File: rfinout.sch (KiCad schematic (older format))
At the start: 4 parts

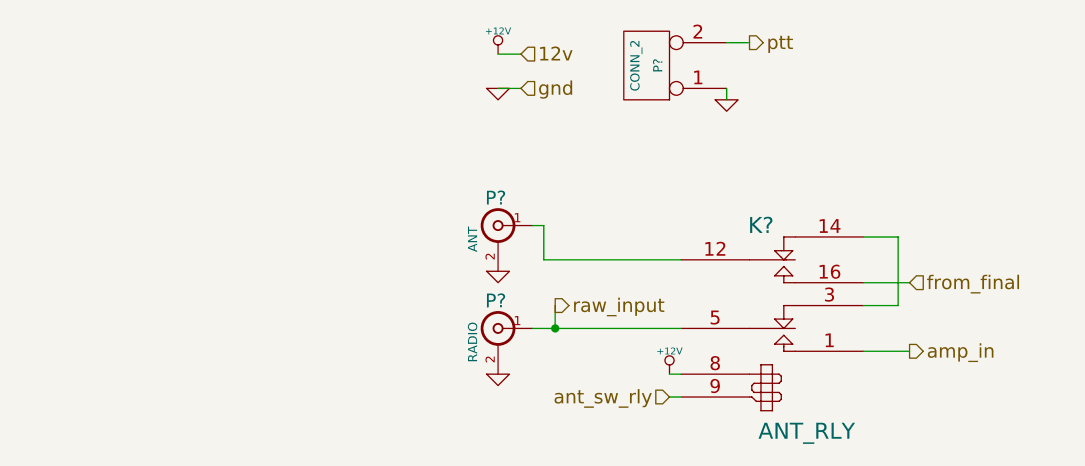
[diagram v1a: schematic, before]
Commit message: Annotated all schematics
- Added more caps to power supply
- Decided on power supply fuse part
- Changed 1n5711 SWR caps to BAT62
- Decided on MMBF170 for amp bias switch
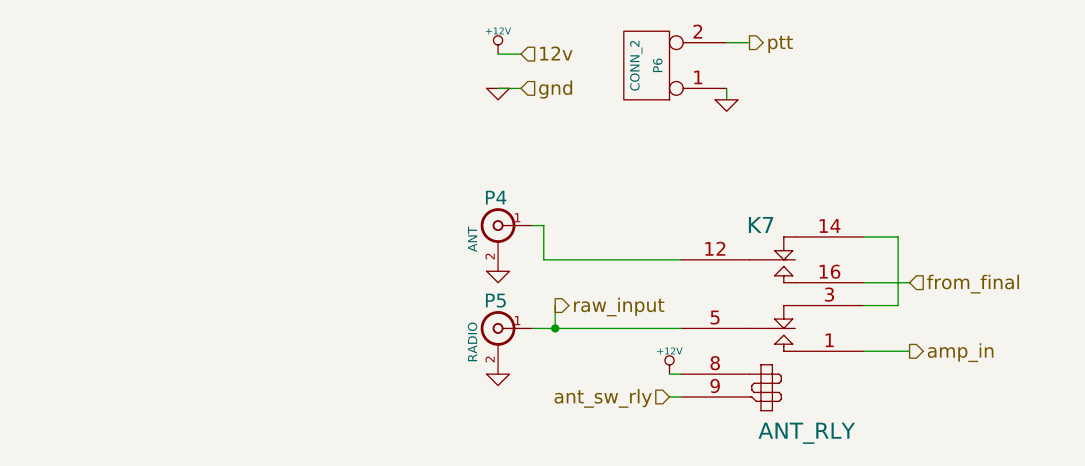
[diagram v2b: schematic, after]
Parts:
- gave numbers to parts that had none: 4
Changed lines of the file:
@@
 $EndDescr
 $Comp
-L BNC P?
+L BNC P5
 U 1 1 5472C36C
 P 5150 3750
-F 0 "P?" H 5160 3870 60  0000 C CNN
+F 0 "P5" H 5160 3870 60  0000 C CNN
 F 1 "RADIO" V 5260 3690 40  0000 C CNN
 F 2 "" H 5150 3750 60  0000 C CNN
@@
 $EndComp
 $Comp
-L BNC P?
+L BNC P4
 U 1 1 5472C37E
 P 5150 3300
-F 0 "P?" H 5160 3420 60  0000 C CNN
+F 0 "P4" H 5160 3420 60  0000 C CNN
 F 1 "ANT" V 5260 3240 40  0000 C CNN
 F 2 "" H 5150 3300 60  0000 C CNN
@@
 $EndComp
 $Comp
-L RELAY_2RT K?
+L RELAY_2RT K7
 U 1 1 5472C38B
 P 6350 3700
-F 0 "K?" H 6300 4100 70  0000 C CNN
+F 0 "K7" H 6300 4100 70  0000 C CNN
 F 1 "ANT_RLY" H 6500 3200 70  0000 C CNN
 F 2 "" H 6350 3700 60  0000 C CNN
@@
 $EndComp
 $Comp
-L +12V #PWR?
+L +12V #PWR100
 U 1 1 5472C39F
 P 5900 3950
-F 0 "#PWR?" H 5900 3900 20  0001 C CNN
+F 0 "#PWR100" H 5900 3900 20  0001 C CNN
 F 1 "+12V" H 5900 4050 30  0000 C CNN
 F 2 "" H 5900 3950 60  0000 C CNN
@@
 ant_sw_rly
 $Comp
-L GND #PWR?
+L GND #PWR99
 U 1 1 5472C3BF
 P 5150 3950
-F 0 "#PWR?" H 5150 3950 30  0001 C CNN
+F 0 "#PWR99" H 5150 3950 30  0001 C CNN
 F 1 "GND" H 5150 3880 30  0001 C CNN
 F 2 "" H 5150 3950 60  0000 C CNN
@@
 $EndComp
 $Comp
-L GND #PWR?
+L GND #PWR98
 U 1 1 5472C3D3
 P 5150 3500
-F 0 "#PWR?" H 5150 3500 30  0001 C CNN
+F 0 "#PWR98" H 5150 3500 30  0001 C CNN
 F 1 "GND" H 5150 3430 30  0001 C CNN
 F 2 "" H 5150 3500 60  0000 C CNN
@@
 from_final
 $Comp
-L GND #PWR?
+L GND #PWR97
 U 1 1 5472C7C7
 P 5150 2700
-F 0 "#PWR?" H 5150 2700 30  0001 C CNN
+F 0 "#PWR97" H 5150 2700 30  0001 C CNN
 F 1 "GND" H 5150 2630 30  0001 C CNN
 F 2 "" H 5150 2700 60  0000 C CNN
@@
 $EndComp
 $Comp
-L +12V #PWR?
+L +12V #PWR96
 U 1 1 5472C7D2
 P 5150 2550
-F 0 "#PWR?" H 5150 2500 20  0001 C CNN
+F 0 "#PWR96" H 5150 2500 20  0001 C CNN
 F 1 "+12V" H 5150 2650 30  0000 C CNN
 F 2 "" H 5150 2550 60  0000 C CNN
@@
 Connection ~ 5400 3750
 $Comp
-L CONN_2 P?
+L CONN_2 P6
 U 1 1 5472CC33
 P 5800 2600
-F 0 "P?" V 5750 2600 40  0000 C CNN
+F 0 "P6" V 5750 2600 40  0000 C CNN
 F 1 "CONN_2" V 5850 2600 40  0000 C CNN
 F 2 "" H 5800 2600 60  0000 C CNN
@@
 $EndComp
 $Comp
-L GND #PWR?
+L GND #PWR101
 U 1 1 5472CC45
 P 6150 2750
-F 0 "#PWR?" H 6150 2750 30  0001 C CNN
+F 0 "#PWR101" H 6150 2750 30  0001 C CNN
 F 1 "GND" H 6150 2680 30  0001 C CNN
 F 2 "" H 6150 2750 60  0000 C CNN

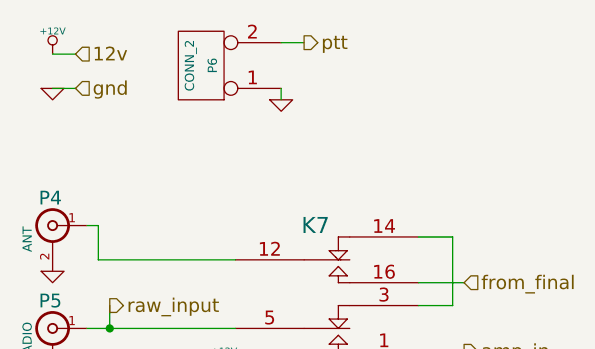
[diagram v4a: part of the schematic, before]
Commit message: Finished associating relays
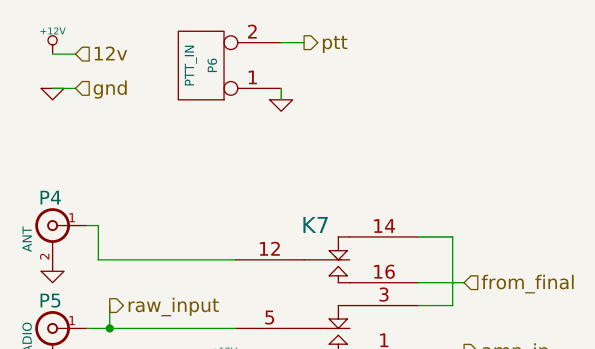
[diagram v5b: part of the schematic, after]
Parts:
- P6: value CONN_2 -> PTT_IN
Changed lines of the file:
@@
 LIBS:mcus
 LIBS:transformers
+LIBS:relays
 LIBS:qrpamp-cache
 EELAYER 25 0
@@
 $EndComp
 $Comp
-L RELAY_2RT K7
-U 1 1 5472C38B
-P 6350 3700
-F 0 "K7" H 6300 4100 70  0000 C CNN
-F 1 "ANT_RLY" H 6500 3200 70  0000 C CNN
-F 2 "" H 6350 3700 60  0001 C CNN
-F 3 "" H 6350 3700 60  0000 C CNN
-	1    6350 3700
-	1    0    0    -1
-$EndComp
-$Comp
-L +12V #PWR096
+L +12V #PWR99
 U 1 1 5472C39F
 P 5900 3950
-F 0 "#PWR096" H 5900 3900 20  0001 C CNN
+F 0 "#PWR99" H 5900 3900 20  0001 C CNN
 F 1 "+12V" H 5900 4050 30  0000 C CNN
 F 2 "" H 5900 3950 60  0000 C CNN
@@
 ant_sw_rly
 $Comp
-L GND #PWR097
+L GND #PWR98
 U 1 1 5472C3BF
 P 5150 3950
-F 0 "#PWR097" H 5150 3950 30  0001 C CNN
+F 0 "#PWR98" H 5150 3950 30  0001 C CNN
 F 1 "GND" H 5150 3880 30  0001 C CNN
 F 2 "" H 5150 3950 60  0000 C CNN
@@
 $EndComp
 $Comp
-L GND #PWR098
+L GND #PWR97
 U 1 1 5472C3D3
 P 5150 3500
-F 0 "#PWR098" H 5150 3500 30  0001 C CNN
+F 0 "#PWR97" H 5150 3500 30  0001 C CNN
 F 1 "GND" H 5150 3430 30  0001 C CNN
 F 2 "" H 5150 3500 60  0000 C CNN
@@
 from_final
 $Comp
-L GND #PWR099
+L GND #PWR96
 U 1 1 5472C7C7
 P 5150 2700
-F 0 "#PWR099" H 5150 2700 30  0001 C CNN
+F 0 "#PWR96" H 5150 2700 30  0001 C CNN
 F 1 "GND" H 5150 2630 30  0001 C CNN
 F 2 "" H 5150 2700 60  0000 C CNN
@@
 $EndComp
 $Comp
-L +12V #PWR0100
+L +12V #PWR95
 U 1 1 5472C7D2
 P 5150 2550
-F 0 "#PWR0100" H 5150 2500 20  0001 C CNN
+F 0 "#PWR95" H 5150 2500 20  0001 C CNN
 F 1 "+12V" H 5150 2650 30  0000 C CNN
 F 2 "" H 5150 2550 60  0000 C CNN
@@
 P 5800 2600
 F 0 "P6" V 5750 2600 40  0000 C CNN
-F 1 "CONN_2" V 5850 2600 40  0000 C CNN
+F 1 "PTT_IN" V 5850 2600 40  0000 C CNN
 F 2 "" H 5800 2600 60  0001 C CNN
 F 3 "" H 5800 2600 60  0000 C CNN
@@
 $EndComp
 $Comp
-L GND #PWR0101
+L GND #PWR100
 U 1 1 5472CC45
 P 6150 2750
-F 0 "#PWR0101" H 6150 2750 30  0001 C CNN
+F 0 "#PWR100" H 6150 2750 30  0001 C CNN
 F 1 "GND" H 6150 2680 30  0001 C CNN
 F 2 "" H 6150 2750 60  0000 C CNN
@@
 Text HLabel 6250 2500 2    60   Output ~ 0
 ptt
+$Comp
+L RELAY_2RT K7
+U 1 1 547A886B
+P 6350 3700
+F 0 "K7" H 6300 4100 70  0000 C CNN
+F 1 "ANT_RLY" H 6500 3200 70  0000 C CNN
+F 2 "" H 6350 3700 60  0000 C CNN
+F 3 "" H 6350 3700 60  0000 C CNN
+	1    6350 3700
+	1    0    0    -1
+$EndComp
 $EndSCHEMATC

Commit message: Everything associated except joystick
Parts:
- K7: footprint (none) -> nu9j-footprints:EC2-12NU
- P4, P5: footprint (none) -> nu9j-footprints:SMA-EDGE-0.375in
- P6: footprint (none) -> nu9j-footprints:3.5MM_SWITCHCRAFT-35RASMT2AHNTRX
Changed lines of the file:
@@
 F 0 "P5" H 5160 3870 60  0000 C CNN
 F 1 "RADIO" V 5260 3690 40  0000 C CNN
-F 2 "" H 5150 3750 60  0001 C CNN
+F 2 "nu9j-footprints:SMA-EDGE-0.375in" H 5150 3750 60  0001 C CNN
 F 3 "" H 5150 3750 60  0000 C CNN
 	1    5150 3750
@@
 F 0 "P4" H 5160 3420 60  0000 C CNN
 F 1 "ANT" V 5260 3240 40  0000 C CNN
-F 2 "" H 5150 3300 60  0001 C CNN
+F 2 "nu9j-footprints:SMA-EDGE-0.375in" H 5150 3300 60  0001 C CNN
 F 3 "" H 5150 3300 60  0000 C CNN
 	1    5150 3300
@@
 $EndComp
 $Comp
-L +12V #PWR99
+L +12V #PWR095
 U 1 1 5472C39F
 P 5900 3950
-F 0 "#PWR99" H 5900 3900 20  0001 C CNN
+F 0 "#PWR095" H 5900 3900 20  0001 C CNN
 F 1 "+12V" H 5900 4050 30  0000 C CNN
 F 2 "" H 5900 3950 60  0000 C CNN
@@
 ant_sw_rly
 $Comp
-L GND #PWR98
+L GND #PWR096
 U 1 1 5472C3BF
 P 5150 3950
-F 0 "#PWR98" H 5150 3950 30  0001 C CNN
+F 0 "#PWR096" H 5150 3950 30  0001 C CNN
 F 1 "GND" H 5150 3880 30  0001 C CNN
 F 2 "" H 5150 3950 60  0000 C CNN
@@
 $EndComp
 $Comp
-L GND #PWR97
+L GND #PWR097
 U 1 1 5472C3D3
 P 5150 3500
-F 0 "#PWR97" H 5150 3500 30  0001 C CNN
+F 0 "#PWR097" H 5150 3500 30  0001 C CNN
 F 1 "GND" H 5150 3430 30  0001 C CNN
 F 2 "" H 5150 3500 60  0000 C CNN
@@
 from_final
 $Comp
-L GND #PWR96
+L GND #PWR098
 U 1 1 5472C7C7
 P 5150 2700
-F 0 "#PWR96" H 5150 2700 30  0001 C CNN
+F 0 "#PWR098" H 5150 2700 30  0001 C CNN
 F 1 "GND" H 5150 2630 30  0001 C CNN
 F 2 "" H 5150 2700 60  0000 C CNN
@@
 $EndComp
 $Comp
-L +12V #PWR95
+L +12V #PWR099
 U 1 1 5472C7D2
 P 5150 2550
-F 0 "#PWR95" H 5150 2500 20  0001 C CNN
+F 0 "#PWR099" H 5150 2500 20  0001 C CNN
 F 1 "+12V" H 5150 2650 30  0000 C CNN
 F 2 "" H 5150 2550 60  0000 C CNN
@@
 F 0 "P6" V 5750 2600 40  0000 C CNN
 F 1 "PTT_IN" V 5850 2600 40  0000 C CNN
-F 2 "" H 5800 2600 60  0001 C CNN
+F 2 "nu9j-footprints:3.5MM_SWITCHCRAFT-35RASMT2AHNTRX" H 5800 2600 60  0001 C CNN
 F 3 "" H 5800 2600 60  0000 C CNN
 	1    5800 2600
@@
 $EndComp
 $Comp
-L GND #PWR100
+L GND #PWR0100
 U 1 1 5472CC45
 P 6150 2750
-F 0 "#PWR100" H 6150 2750 30  0001 C CNN
+F 0 "#PWR0100" H 6150 2750 30  0001 C CNN
 F 1 "GND" H 6150 2680 30  0001 C CNN
 F 2 "" H 6150 2750 60  0000 C CNN
@@
 F 0 "K7" H 6300 4100 70  0000 C CNN
 F 1 "ANT_RLY" H 6500 3200 70  0000 C CNN
-F 2 "" H 6350 3700 60  0000 C CNN
+F 2 "nu9j-footprints:EC2-12NU" H 6350 3700 60  0001 C CNN
 F 3 "" H 6350 3700 60  0000 C CNN
 	1    6350 3700

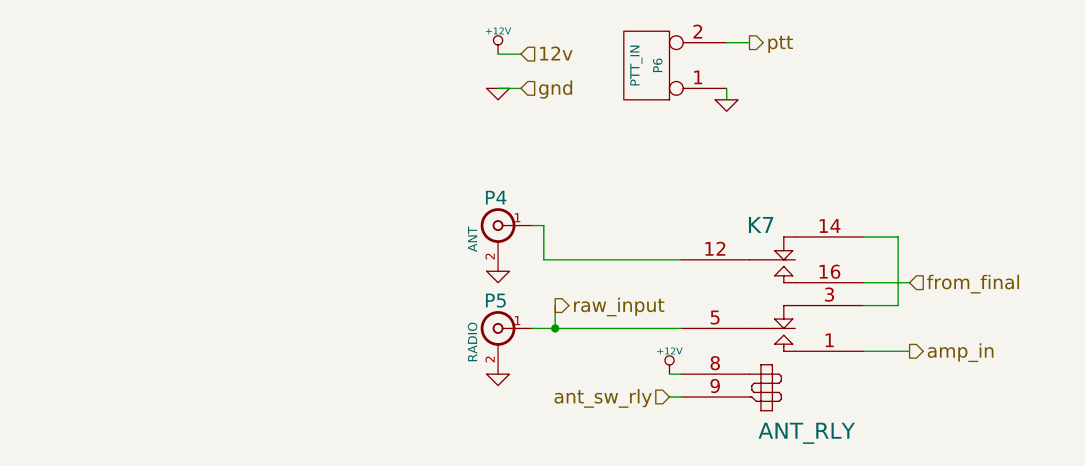
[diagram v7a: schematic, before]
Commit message: Note about SMA connector part number
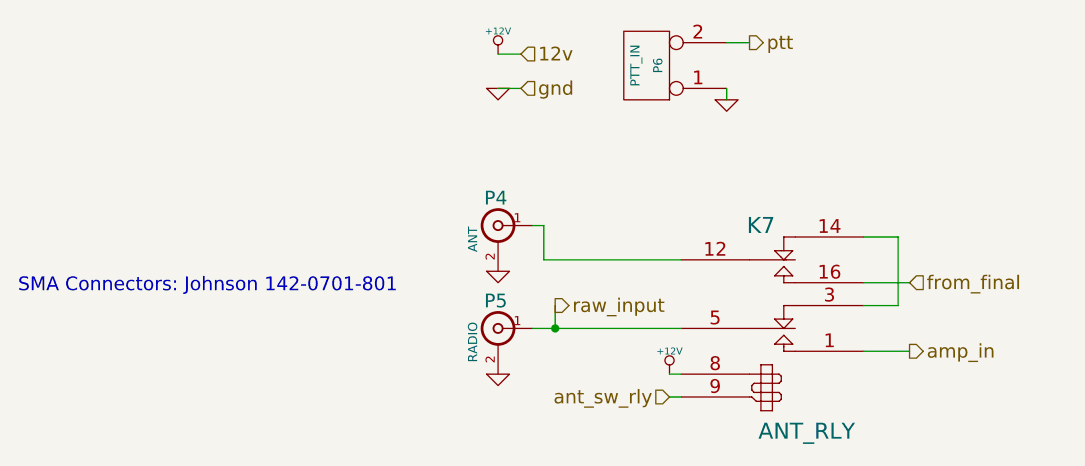
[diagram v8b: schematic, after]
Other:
- note added: "SMA Connectors: Johnson 142-0701-801"
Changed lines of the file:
@@
 	1    0    0    -1
 $EndComp
+Text Notes 3050 3600 0    60   ~ 0
+SMA Connectors: Johnson 142-0701-801
 $EndSCHEMATC
